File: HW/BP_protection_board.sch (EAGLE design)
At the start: 39 parts, among them IC1 74AC08D, K1 G5LE, K2 G5LE, Q1 2N7002, Q2 2N7002

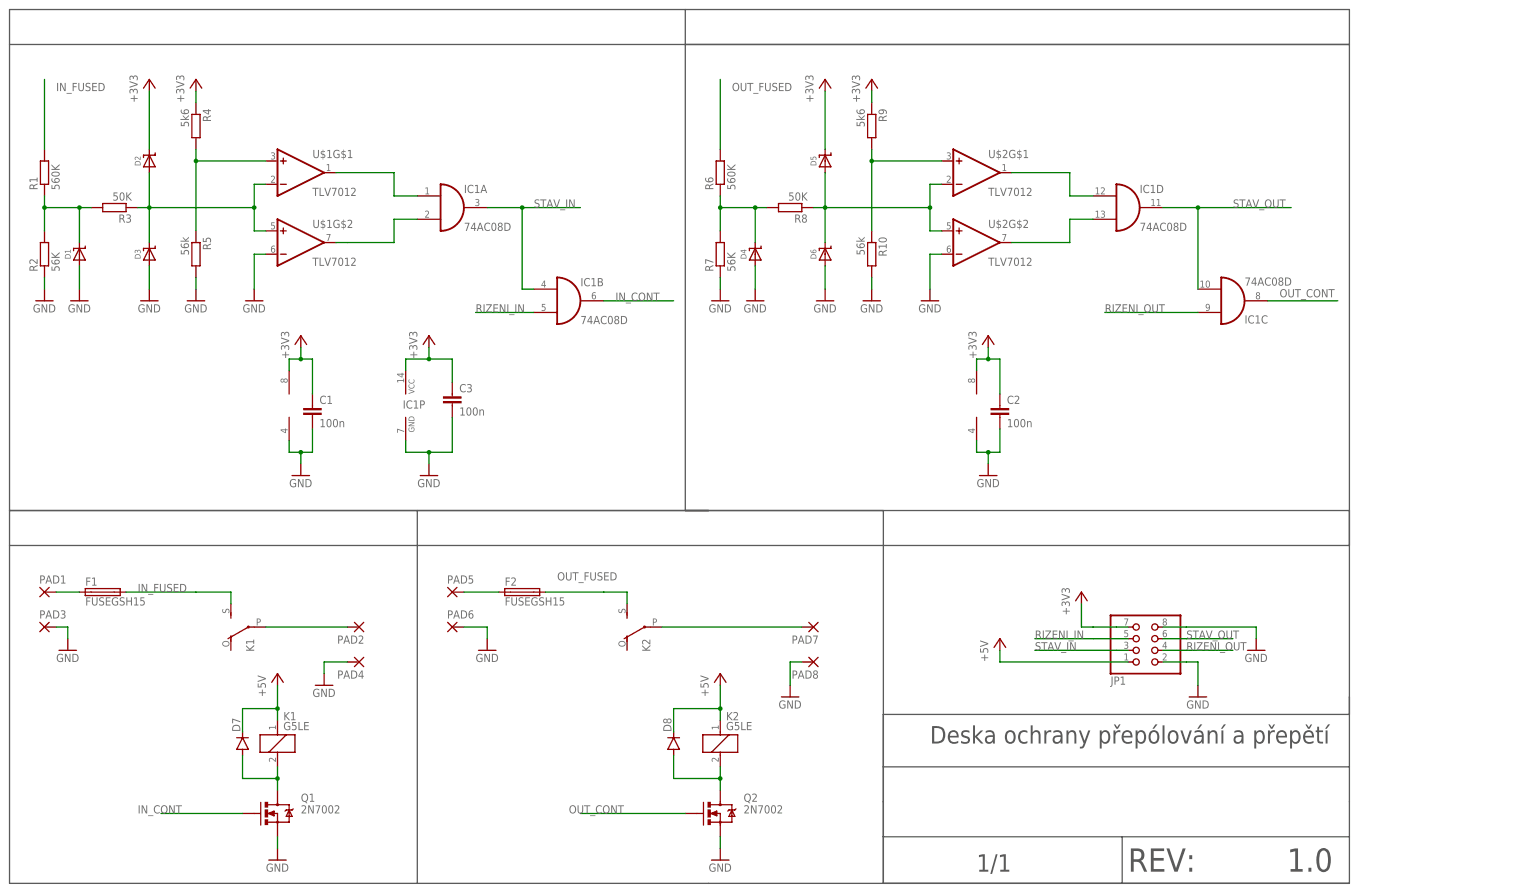
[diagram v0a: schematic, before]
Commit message: Přidáno propojení desek fastony a distančními sloupky, změněna logika vyhodnocení nežádoucích stavů
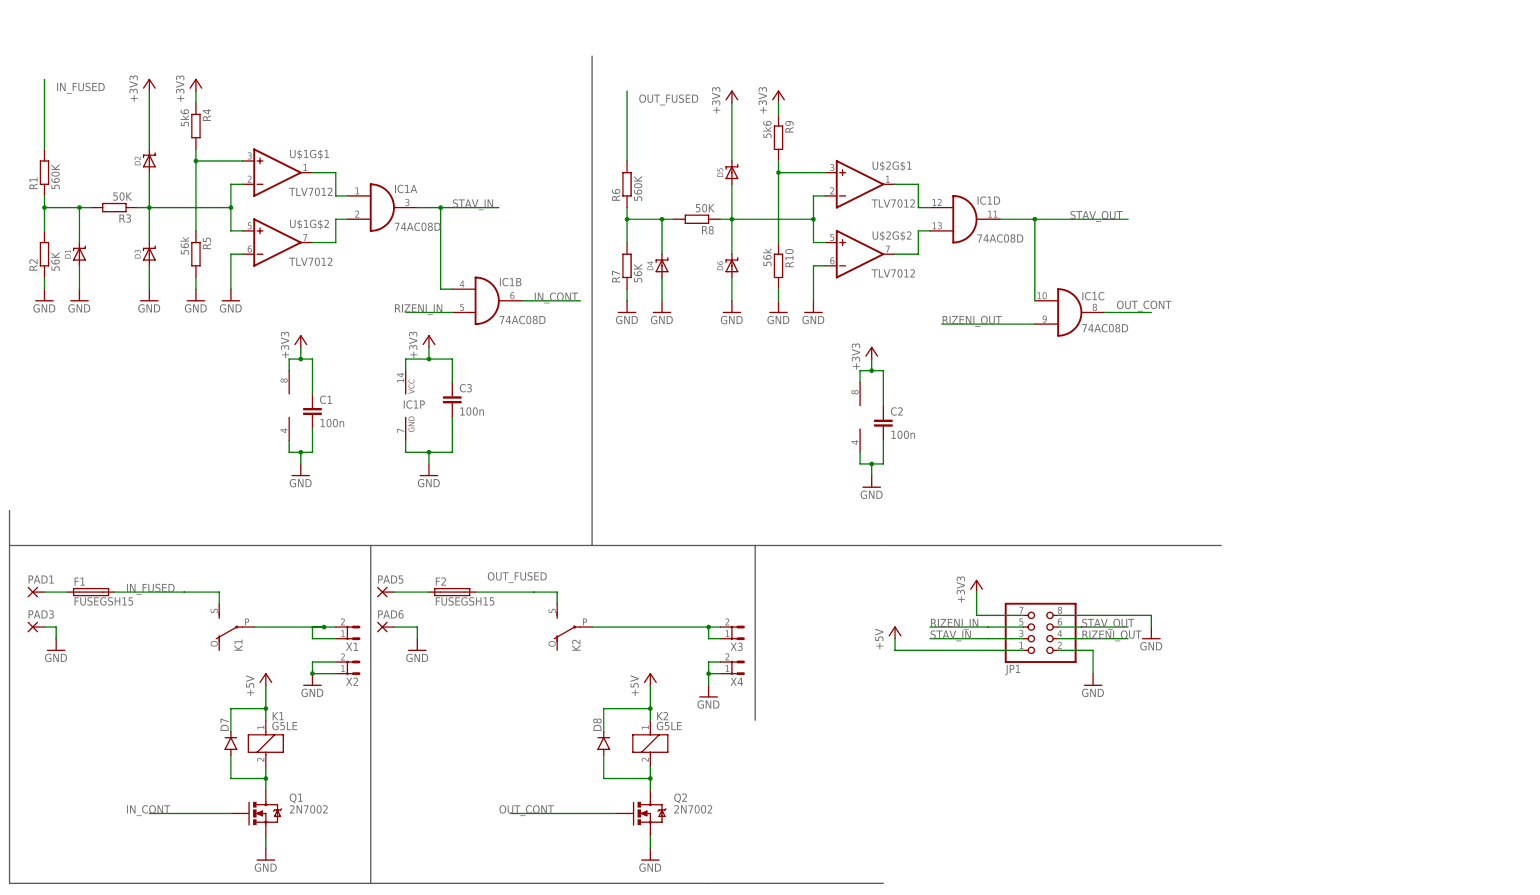
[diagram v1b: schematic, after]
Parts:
- removed PAD2, PAD4, PAD7, PAD8: (no value), wirepad:2,54/1,0
- added X1, X2, X3, X4: (no value), con-rib:ST6,3
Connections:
- net GND: now also X2.1, X2.2, X4.1, X4.2; no longer PAD4.P, PAD8.P
- net N$8: now also X1.1, X1.2; no longer PAD2.P
- net N$9: now also X3.1, X3.2; no longer PAD7.P
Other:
- note removed: "1/1"
- note removed: "Deska ochrany přepólování a přepětí"
- note removed: "REV: 1.0"
- moved on the sheet: C2, D4, D5, D6, D7, D8, F1, F2, IC1A, IC1B, IC1C, IC1D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
